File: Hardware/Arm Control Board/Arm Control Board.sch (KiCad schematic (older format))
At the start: 32 parts, among them P1 Servo 1, P10 UIM240XX_Stepper_Conn, P11 Battery, P12 SyRen, P13 Raspberry Pi, P14 Gripper Force Fdbk, P2 Shoulder Feedback, P3 Servo 2, P4 Servo 3, P5 Elbow Feedback, P6 Servo 4, P7 RS485, P8 ST_SWD_Connector, P9 Servo 5, U1 STM32F401RCT6, U2 SN75176BDR, U3 74LVCH244APW, X1 24MHz

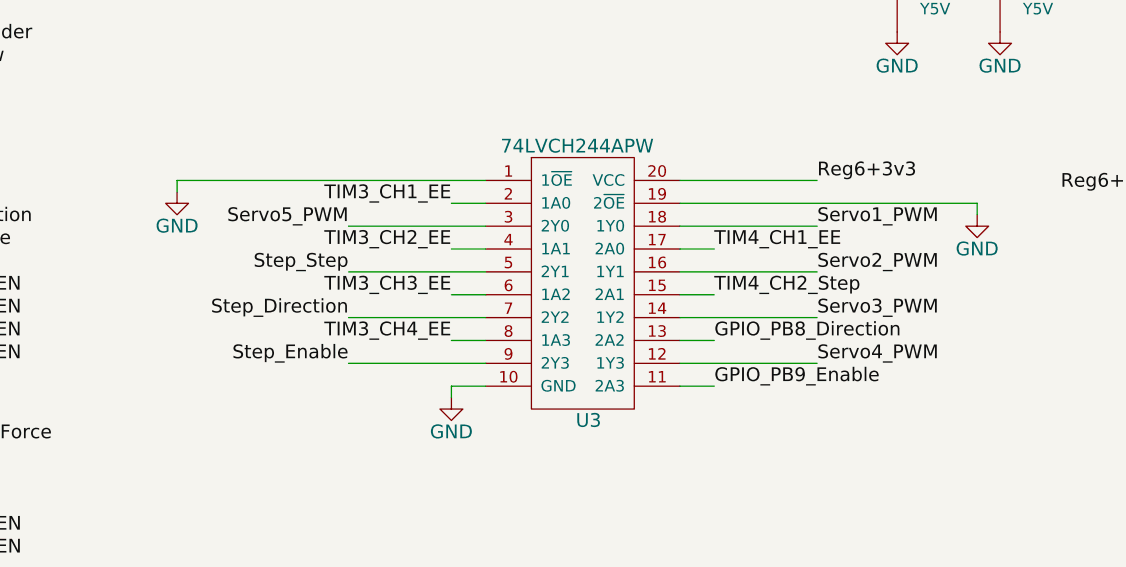
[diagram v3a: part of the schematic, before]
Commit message: Reorganize all regulators. Reorganize buffer pins
Pins reorganized to simplify board flow
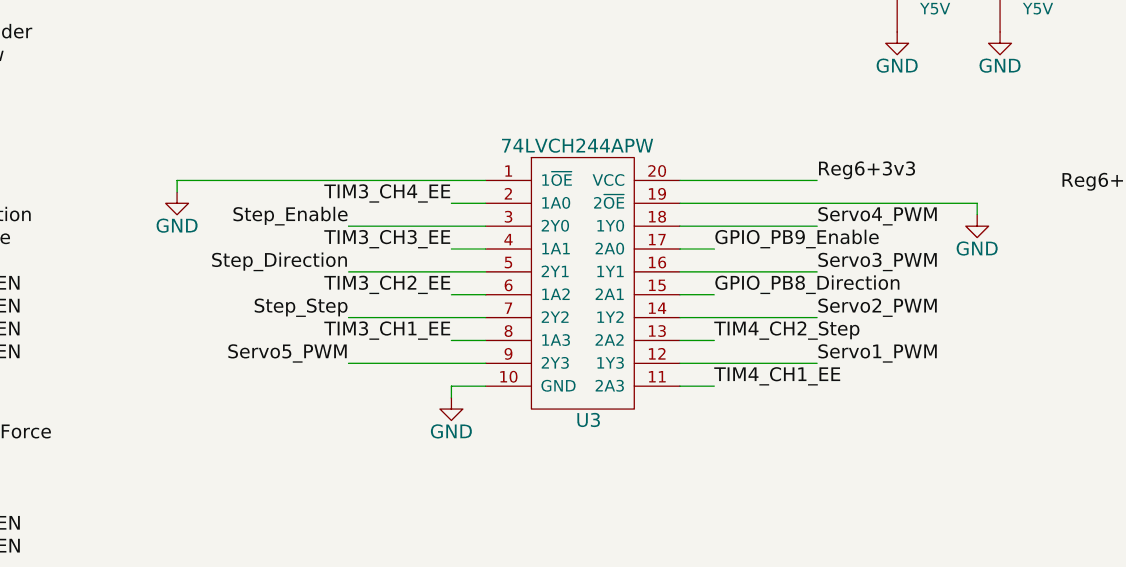
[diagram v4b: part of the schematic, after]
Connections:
- net GPIO_PB8_Direction: now also U3.15 (2A1); no longer U3.13 (2A2)
- net GPIO_PB9_Enable: now also U3.17 (2A0); no longer U3.11 (2A3)
- net Servo1_PWM: now also U3.12 (1Y3); no longer U3.18 (1Y0)
- net Servo2_PWM: now also U3.14 (1Y2); no longer U3.16 (1Y1)
- net Servo3_PWM: now also U3.16 (1Y1); no longer U3.14 (1Y2)
- net Servo4_PWM: now also U3.18 (1Y0); no longer U3.12 (1Y3)
- net Servo5_PWM: now also U3.9 (2Y3); no longer U3.3 (2Y0)
- net Step_Direction: now also U3.5 (2Y1); no longer U3.7 (2Y2)
- net Step_Enable: now also U3.3 (2Y0); no longer U3.9 (2Y3)
- net Step_Step: now also U3.7 (2Y2); no longer U3.5 (2Y1)
- net TIM3_CH1_EE: now also U3.8 (1A3); no longer U3.2 (1A0)
- net TIM3_CH2_EE: now also U3.6 (1A2); no longer U3.4 (1A1)
- net TIM3_CH3_EE: now also U3.4 (1A1); no longer U3.6 (1A2)
- net TIM3_CH4_EE: now also U3.2 (1A0); no longer U3.8 (1A3)
- net TIM4_CH1_EE: now also U3.11 (2A3); no longer U3.17 (2A0)
- net TIM4_CH2_Step: now also U3.13 (2A2); no longer U3.15 (2A1)
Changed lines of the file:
@@
 Text Label 5600 3400 0    60   ~ 0
 Reg6+3v3
-Text Label 5600 3600 0    60   ~ 0
+Text Label 5600 4200 0    60   ~ 0
 Servo1_PWM
 Text Label 1150 6900 0    60   ~ 0
@@
 Text Label 1350 5150 0    60   ~ 0
 TIM3_CH1_EE
-Text Label 4000 3500 2    60   ~ 0
+Text Label 4000 4100 2    60   ~ 0
 TIM3_CH1_EE
 Text Label 1350 5250 0    60   ~ 0
 TIM3_CH2_EE
-Text Label 4000 3700 2    60   ~ 0
+Text Label 4000 3900 2    60   ~ 0
 TIM3_CH2_EE
 Text Label 1350 5350 0    60   ~ 0
 TIM3_CH3_EE
-Text Label 4000 3900 2    60   ~ 0
+Text Label 4000 3700 2    60   ~ 0
 TIM3_CH3_EE
 Text Label 1350 5450 0    60   ~ 0
 TIM3_CH4_EE
-Text Label 5600 4000 0    60   ~ 0
+Text Label 5600 3800 0    60   ~ 0
 Servo3_PWM
-Text Label 5600 4200 0    60   ~ 0
+Text Label 5600 3600 0    60   ~ 0
 Servo4_PWM
 Text Label 1350 3400 0    60   ~ 0
 TIM4_CH1_EE
-Text Label 5150 3700 0    60   ~ 0
+Text Label 5150 4300 0    60   ~ 0
 TIM4_CH1_EE
-Text Label 3550 3600 2    60   ~ 0
+Text Label 3550 4200 2    60   ~ 0
 Servo5_PWM
 $Comp
@@
 Text Label 1350 3700 0    60   ~ 0
 GPIO_PB9_Enable
-Text Label 4000 4100 2    60   ~ 0
+Text Label 4000 3500 2    60   ~ 0
 TIM3_CH4_EE
-Text Label 5600 3800 0    60   ~ 0
+Text Label 5600 4000 0    60   ~ 0
 Servo2_PWM
-Text Label 5150 3900 0    60   ~ 0
+Text Label 5150 4100 0    60   ~ 0
 TIM4_CH2_Step
 Text Label 7950 5000 2    60   ~ 0
@@
 Text Label 7950 5200 2    60   ~ 0
 Step_Enable
+Text Label 3550 4000 2    60   ~ 0
+Step_Step
+Text Label 5150 3900 0    60   ~ 0
+GPIO_PB8_Direction
+Text Label 5150 3700 0    60   ~ 0
+GPIO_PB9_Enable
 Text Label 3550 3800 2    60   ~ 0
-Step_Step
-Text Label 5150 4100 0    60   ~ 0
-GPIO_PB8_Direction
-Text Label 5150 4300 0    60   ~ 0
-GPIO_PB9_Enable
-Text Label 3550 4000 2    60   ~ 0
 Step_Direction
-Text Label 3550 4200 2    60   ~ 0
+Text Label 3550 3600 2    60   ~ 0
 Step_Enable
 $Comp

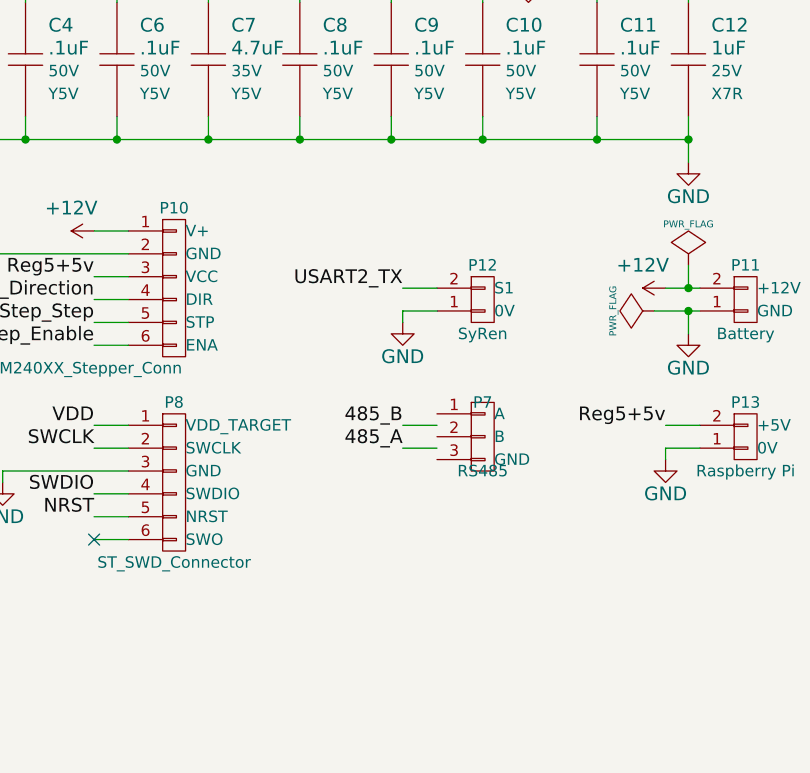
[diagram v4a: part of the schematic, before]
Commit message: Add terminating resistance for 485, add 232 header
Resolves #23  #22
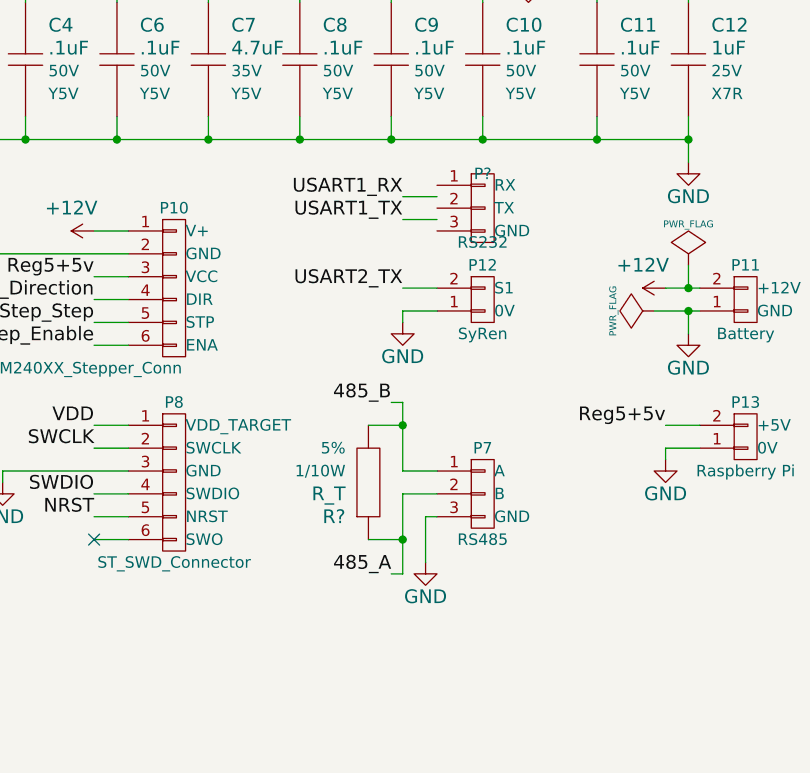
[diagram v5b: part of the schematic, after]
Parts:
- added P?: RS232, symbol RS232
- added R?: R_T, symbol Resistor
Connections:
- net 485_A: now also P7.2 (B), R?.1
- net 485_B: now also P7.1 (A), R?.2
- net GND: now also P7.3 (GND)
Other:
- moved on the sheet: P7
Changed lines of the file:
@@
 L RS485 P7
 U 1 1 54C47C8E
-P 9650 5600
-F 0 "P7" H 9650 5750 50  0000 C CNN
-F 1 "RS485" H 9650 5450 50  0000 C CNN
-F 2 "MAVRIC_footprints:1x2_SMD_header" H 9650 5600 60  0001 C CNN
-F 3 "" H 9650 5600 60  0000 C CNN
-	1    9650 5600
+P 9650 5850
+F 0 "P7" H 9650 6050 50  0000 C CNN
+F 1 "RS485" H 9650 5650 50  0000 C CNN
+F 2 "MAVRIC_footprints:1x2_SMD_header" H 9650 5850 60  0001 C CNN
+F 3 "" H 9650 5850 60  0000 C CNN
+	1    9650 5850
 	1    0    0    -1
 $EndComp
@@
 Text Label 4150 1300 0    60   ~ 0
 485_A
-Wire Wire Line
-	9450 5550 9300 5550
-Wire Wire Line
-	9450 5650 9300 5650
-Text Label 9300 5550 2    60   ~ 0
+Text Label 9250 5450 2    60   ~ 0
 485_B
-Text Label 9300 5650 2    60   ~ 0
-485_A
 $Comp
 L Actuator_Pot P14
@@
 Text Label 5250 5900 0    60   ~ 0
 ADC1_IN10_GripForce
+Wire Wire Line
+	9300 5750 9450 5750
+Wire Wire Line
+	9450 5850 9300 5850
+Wire Wire Line
+	9450 5950 9400 5950
+Wire Wire Line
+	9400 5950 9400 6150
+$Comp
+L GND #PWR?
+U 1 1 54E4E142
+P 9400 6150
+F 0 "#PWR?" H 9400 5900 60  0001 C CNN
+F 1 "GND" H 9400 6000 60  0000 C CNN
+F 2 "" H 9400 6150 60  0000 C CNN
+F 3 "" H 9400 6150 60  0000 C CNN
+	1    9400 6150
+	1    0    0    -1
+$EndComp
+Text Label 9250 6200 2    60   ~ 0
+485_A
+Wire Wire Line
+	9300 5850 9300 6200
+Wire Wire Line
+	9300 6200 9250 6200
+Wire Wire Line
+	9250 5450 9300 5450
+Wire Wire Line
+	9300 5450 9300 5750
+$Comp
+L Resistor R?
+U 1 1 54E522EE
+P 9150 5800
+F 0 "R?" V 9000 5900 60  0000 L CNN
+F 1 "R_T" V 9100 5900 60  0000 L CNN
+F 2 "" H 9050 5800 60  0001 C CNN
+F 3 "" H 9150 5900 60  0001 C CNN
+F 4 "Value" H 9150 5800 60  0001 C CNN "Manufacturer"
+F 5 "Value" H 9150 5800 60  0001 C CNN "Manufacturer Part #"
+F 6 "Value" H 9150 5800 60  0001 C CNN "Vendor"
+F 7 "Value" H 9150 5800 60  0001 C CNN "Vendor Part #"
+F 8 "1/10W" V 9200 5900 50  0000 L CNN "Power"
+F 9 "5%" V 9300 5900 50  0000 L CNN "Tolerance"
+	1    9150 5800
+	0    -1   -1   0
+$EndComp
+Wire Wire Line
+	9150 5550 9300 5550
+Connection ~ 9300 5550
+Wire Wire Line
+	9150 6050 9300 6050
+Connection ~ 9300 6050
+Text Label 9300 4650 2    60   ~ 0
+USART1_TX
+Text Label 9300 4550 2    60   ~ 0
+USART1_RX
+$Comp
+L RS232 P?
+U 1 1 54E5BB0C
+P 9650 4600
+F 0 "P?" H 9650 4750 50  0000 C CNN
+F 1 "RS232" H 9650 4450 50  0000 C CNN
+F 2 "" H 9650 4600 60  0000 C CNN
+F 3 "" H 9650 4600 60  0000 C CNN
+	1    9650 4600
+	1    0    0    -1
+$EndComp
+Wire Wire Line
+	9450 4550 9300 4550
+Wire Wire Line
+	9300 4650 9450 4650
 $EndSCHEMATC

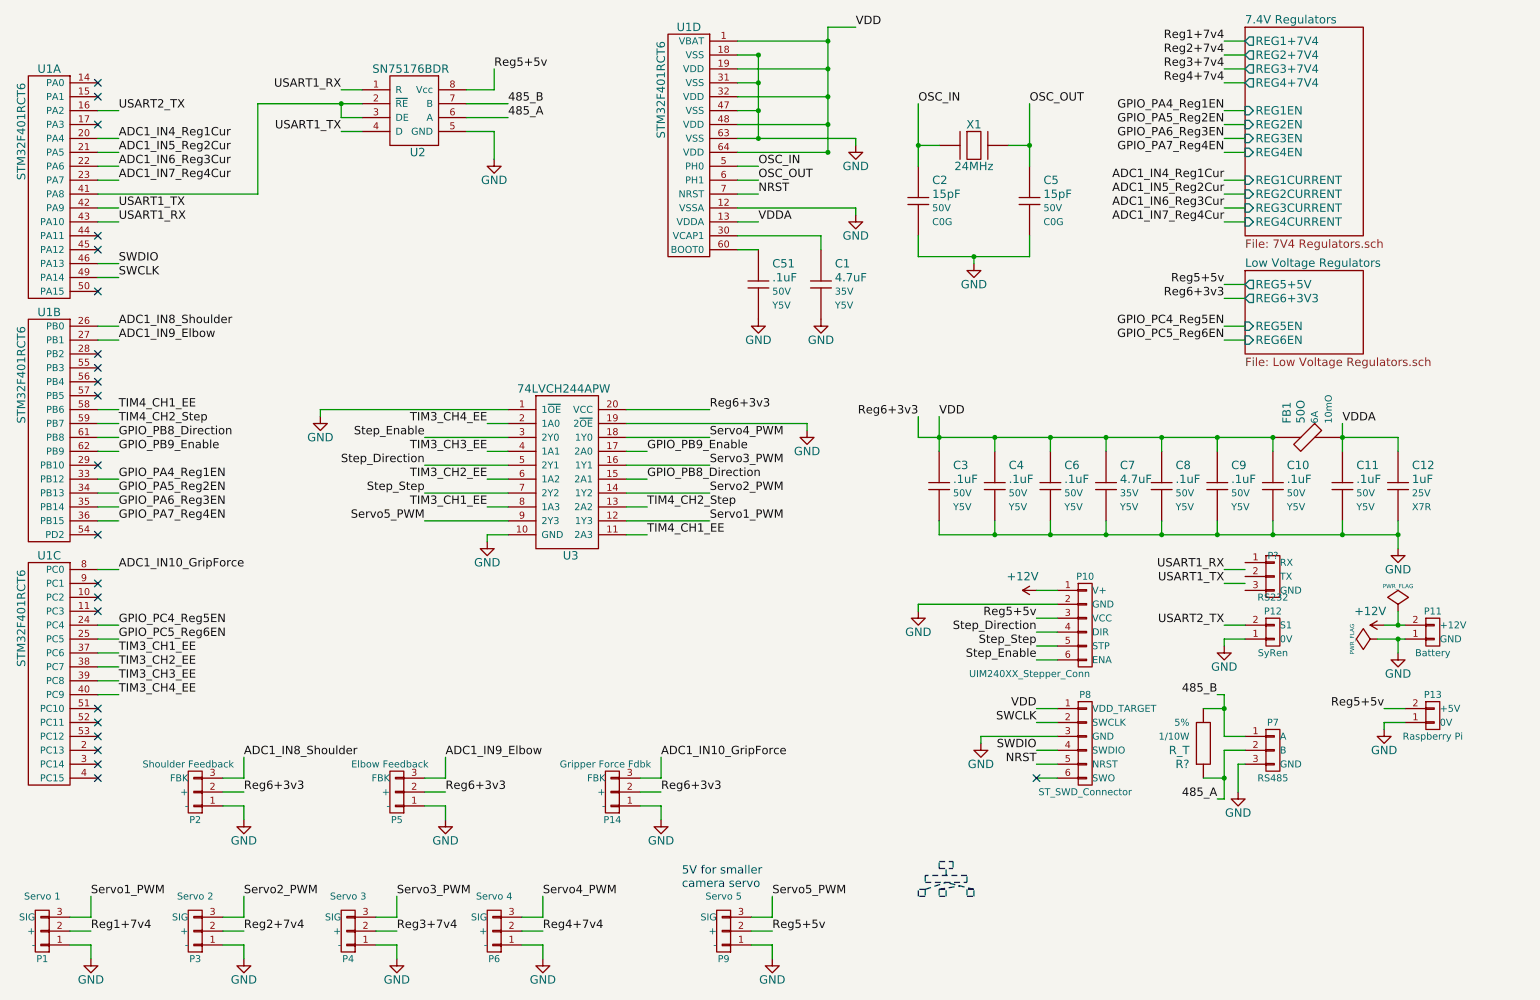
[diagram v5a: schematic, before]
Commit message: Add value for terminating resistance on 485
#24
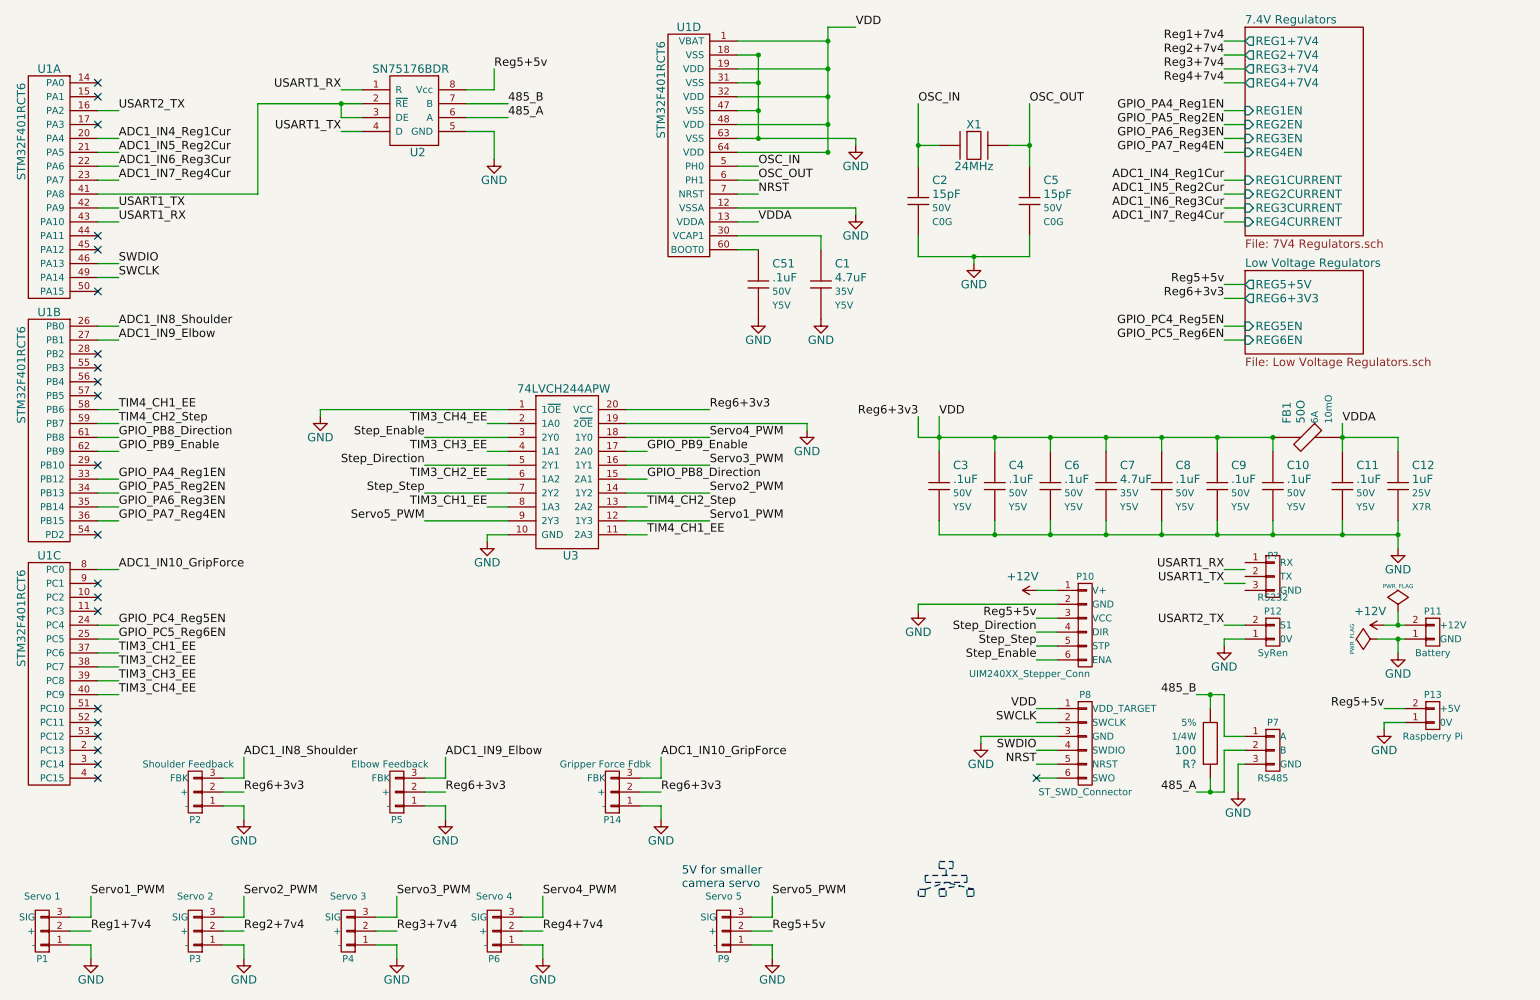
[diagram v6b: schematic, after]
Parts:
- R?: value R_T -> 100; footprint (none) -> Resistors_SMD:R_1206_HandSoldering; Manufacturer Value -> Panasonic; Manufacturer Part # Value -> ERJ-8GEYJ101V; Power 1/10W -> 1/4W; Vendor Value -> Digi-Key; Vendor Part # Value -> P100ECT-ND
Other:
- moved on the sheet: R?
